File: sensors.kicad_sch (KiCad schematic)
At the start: 52 parts, among them Q10 IBLML6344, Q11 IBLML6344, Q4 IBLML6344, Q5 BC817-40, Q6 BC817-40, Q7 IBLML6344, Q8 BC817-40, Q9 BC817-40

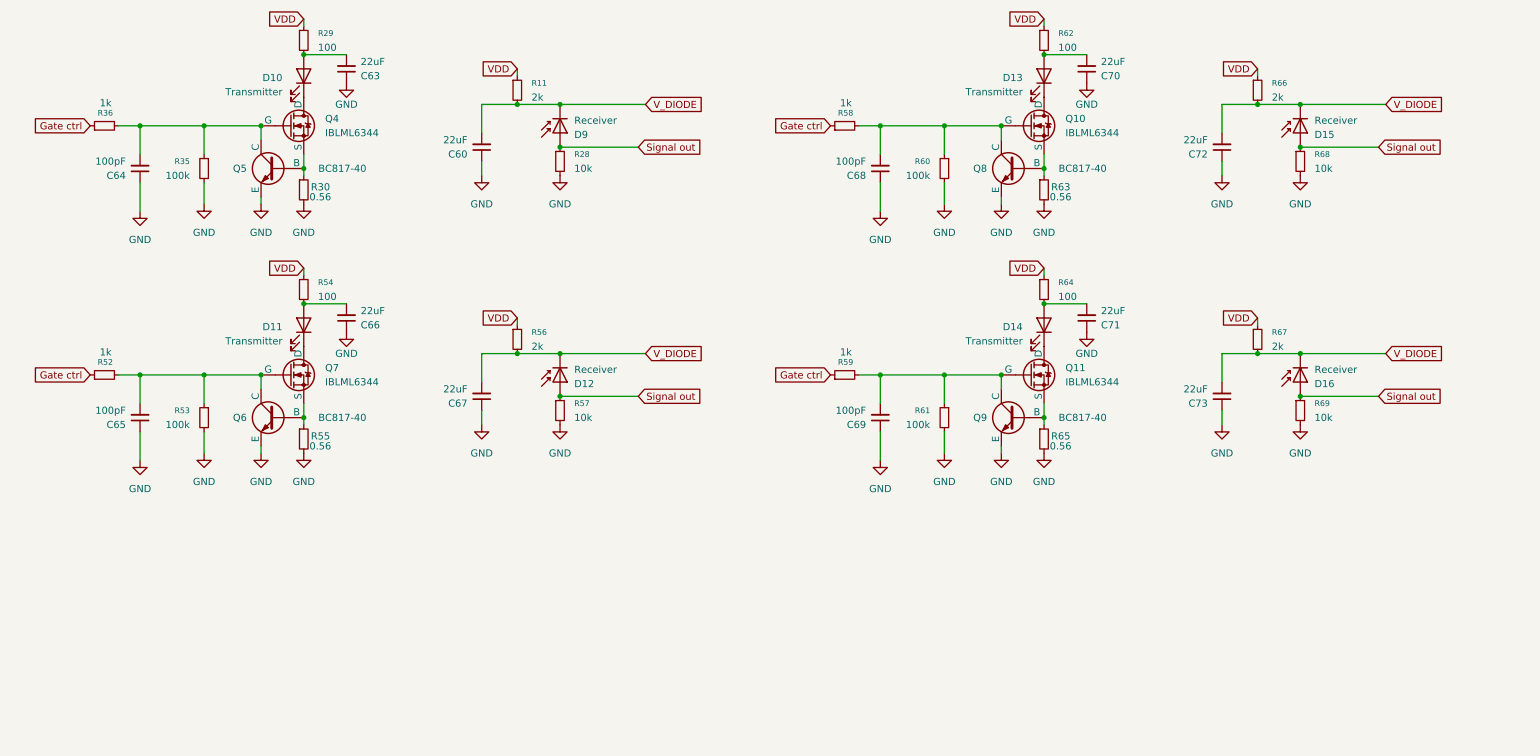
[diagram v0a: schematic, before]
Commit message: fixed sensor schematic and begun pcb layout
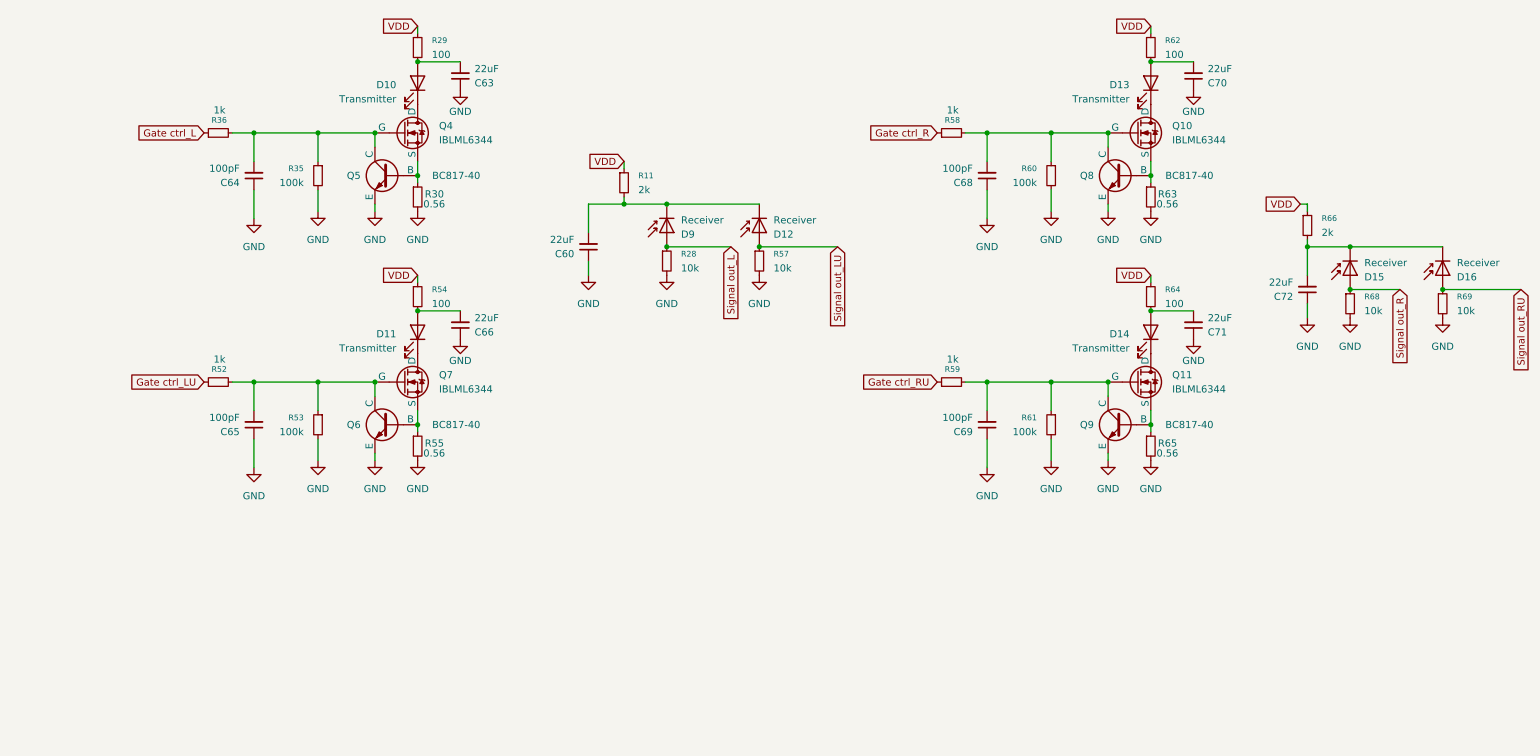
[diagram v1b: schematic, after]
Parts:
- removed C67, C73: 22uF, Capacitor_SMD:C_0805_2012Metric_Pad1.18x1.45mm_HandSolder, symbol Device:C_Small
- removed R56, R67: 2k, Resistor_SMD:R_0805_2012Metric_Pad1.20x1.40mm_HandSolder, symbol Device:R_Small
- D10, D11, D12, D13, D14, D15, D16, D9: footprint (none) -> Connector_PinHeader_2.54mm:PinHeader_1x02_P2.54mm_Vertical
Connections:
- removed net Gate ctrl: R36.1, R52.1, R58.1, R59.1
- removed net Signal out: D12.2 (A), D15.2 (A), D16.2 (A), D9.2 (A), R28.1, R57.1, R68.1, R69.1
- net V_DIODE: no longer names the net of C72.2, D15.1 (K), D16.1 (K), R66.2
- net V_DIODE: no longer C60.2, D12.1 (K), D9.1 (K), R11.2
- new net: C60.2, D12.1 (K), D9.1 (K), R11.2
- new net Gate ctrl_L: R36.1
- new net Gate ctrl_LU: R52.1
- new net Gate ctrl_R: R58.1
- new net Gate ctrl_RU: R59.1
- new net Signal out_L: D9.2 (A), R28.1
- new net Signal out_LU: D12.2 (A), R57.1
- new net Signal out_R: D15.2 (A), R68.1
- new net Signal out_RU: D16.2 (A), R69.1
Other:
- moved on the sheet: C60, C63, C64, C65, C66, C68, C69, C70, C71, C72, D10, D11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

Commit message: slightly change schematic, making sure everything is ok, preparing for finalization
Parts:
- added J11, J12: Conn_01x04, Connector_PinHeader_2.54mm:PinHeader_1x04_P2.54mm_Vertical, symbol Connector_Generic:Conn_01x04
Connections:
- net GND: now also J11.4 (Pin_4), J12.4 (Pin_4)
- new net +3V3: J11.1 (Pin_1), J12.1 (Pin_1)
- new net SIG1: J11.2 (Pin_2)
- new net SIG2: J11.3 (Pin_3)
- new net SIG3: J12.2 (Pin_2)
- new net SIG4: J12.3 (Pin_3)
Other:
- note added: "LEFT AND LEFT-UPPER SENSORS"
- note added: "RIGHT AND RIGHT-UPPER SENSORS"
- note added: "ROTARY ENCODERS"
- moved on the sheet: C60, C63, C64, C65, C66, C68, C69, C70, C71, C72, D10, D11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
